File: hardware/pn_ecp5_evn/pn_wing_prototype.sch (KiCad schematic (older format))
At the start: 7 parts, among them J101 Screw_Terminal_01x02, J102 Conn_Coaxial, J103 Conn_02x20_Odd_Even, J104 Conn_Coaxial, J105 Conn_Coaxial, J106 Conn_Coaxial, J107 Conn_01x10

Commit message: first pass footprint assignment on pn r0
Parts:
- J101: footprint (none) -> TerminalBlock_Phoenix:TerminalBlock_Phoenix_MPT-0,5-2-2.54_1x02_P2.54mm_Horizontal
- J102: footprint (none) -> Connector_Coaxial:SMA_Molex_73251-1153_EdgeMount_Horizontal
- J103: footprint (none) -> Connector_PinSocket_2.54mm:PinSocket_2x20_P2.54mm_Vertical
- J104, J105, J106: footprint (none) -> Connector_Coaxial:SMA_Amphenol_132134_Vertical
- J107: footprint (none) -> Connector_PinHeader_2.54mm:PinHeader_1x10_P2.54mm_Vertical
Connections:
- net isolator/BUF_~PD~_ISO: now reaches J103.31 (Pin_31)
- no-connect marks 12 -> 11
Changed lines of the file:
@@
 F 0 "J102" H 1078 1988 50  0000 C CNN
 F 1 "Conn_Coaxial" H 1078 1897 50  0000 C CNN
-F 2 "" H 1150 1750 50  0001 C CNN
+F 2 "Connector_Coaxial:SMA_Molex_73251-1153_EdgeMount_Horizontal" H 1150 1750 50  0001 C CNN
 F 3 " ~" H 1150 1750 50  0001 C CNN
 	1    1150 1750
@@
 F4 "VOUT_P" I R 6700 1650 50
 F5 "VOUT_N" I R 6700 2150 50
+F6 "BUF_~PD" I R 6700 3050 50
 $EndSheet
 $Sheet
@@
 F20 "ADC_SCK" I R 7650 5250 50
 F21 "ADC_SDO" O R 7650 5350 50
+F22 "BUF_~PD" I L 6550 5450 50
+F23 "BUF_~PD~_ISO" O R 7650 5450 50
 $EndSheet
 Text Label 6350 3950 2    50   ~ 0
@@
 F 0 "J104" H 9250 1625 50  0000 L CNN
 F 1 "Conn_Coaxial" H 9250 1534 50  0000 L CNN
-F 2 "" H 9150 1650 50  0001 C CNN
+F 2 "Connector_Coaxial:SMA_Amphenol_132134_Vertical" H 9150 1650 50  0001 C CNN
 F 3 " ~" H 9150 1650 50  0001 C CNN
 	1    9150 1650
@@
 F 0 "J105" H 9250 2125 50  0000 L CNN
 F 1 "Conn_Coaxial" H 9250 2034 50  0000 L CNN
-F 2 "" H 9150 2150 50  0001 C CNN
+F 2 "Connector_Coaxial:SMA_Amphenol_132134_Vertical" H 9150 2150 50  0001 C CNN
 F 3 " ~" H 9150 2150 50  0001 C CNN
 	1    9150 2150
@@
 F 0 "J106" H 9250 2675 50  0000 L CNN
 F 1 "Conn_Coaxial" H 9250 2584 50  0000 L CNN
-F 2 "" H 9150 2700 50  0001 C CNN
+F 2 "Connector_Coaxial:SMA_Amphenol_132134_Vertical" H 9150 2700 50  0001 C CNN
 F 3 " ~" H 9150 2700 50  0001 C CNN
 	1    9150 2700
@@
 F 0 "J103" H 9100 5967 50  0000 C CNN
 F 1 "Conn_02x20_Odd_Even" H 9100 5876 50  0000 C CNN
-F 2 "" H 9050 4850 50  0001 C CNN
+F 2 "Connector_PinSocket_2.54mm:PinSocket_2x20_P2.54mm_Vertical" H 9050 4850 50  0001 C CNN
 F 3 "~" H 9050 4850 50  0001 C CNN
 	1    9050 4850
@@
 F 0 "J107" H 10150 4950 50  0000 L CNN
 F 1 "Conn_01x10" H 10050 4850 50  0000 L CNN
-F 2 "" H 10200 4350 50  0001 C CNN
+F 2 "Connector_PinHeader_2.54mm:PinHeader_1x10_P2.54mm_Vertical" H 10200 4350 50  0001 C CNN
 F 3 "~" H 10200 4350 50  0001 C CNN
 	1    10200 4350
@@
 NoConn ~ 8850 4250
 NoConn ~ 8850 4950
-NoConn ~ 8850 5450
 NoConn ~ 8850 5550
 NoConn ~ 8850 5650
@@
 F 0 "J101" H 1080 5342 50  0000 L CNN
 F 1 "Screw_Terminal_01x02" H 1080 5251 50  0000 L CNN
-F 2 "" H 1000 5350 50  0001 C CNN
+F 2 "TerminalBlock_Phoenix:TerminalBlock_Phoenix_MPT-0,5-2-2.54_1x02_P2.54mm_Horizontal" H 1000 5350 50  0001 C CNN
 F 3 "~" H 1000 5350 50  0001 C CNN
 	1    1000 5350
@@
 Wire Wire Line
 	1200 5350 1400 5350
+Wire Wire Line
+	7650 5450 8850 5450
+Wire Wire Line
+	6550 5450 6350 5450
+Text Label 6350 5450 2    50   ~ 0
+BUF_~PD
+Text Label 6850 3050 0    50   ~ 0
+BUF_~PD
+Wire Wire Line
+	6850 3050 6700 3050
 $EndSCHEMATC

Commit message: started component placement on phase noise analyzer
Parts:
- J102: footprint Connector_Coaxial:SMA_Molex_73251-1153_EdgeMount_Horizontal -> vna:SMA_Molex_73251-1153_OSHFR408
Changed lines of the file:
@@
 F 0 "J102" H 1078 1988 50  0000 C CNN
 F 1 "Conn_Coaxial" H 1078 1897 50  0000 C CNN
-F 2 "Connector_Coaxial:SMA_Molex_73251-1153_EdgeMount_Horizontal" H 1150 1750 50  0001 C CNN
+F 2 "vna:SMA_Molex_73251-1153_OSHFR408" H 1150 1750 50  0001 C CNN
 F 3 " ~" H 1150 1750 50  0001 C CNN
 	1    1150 1750

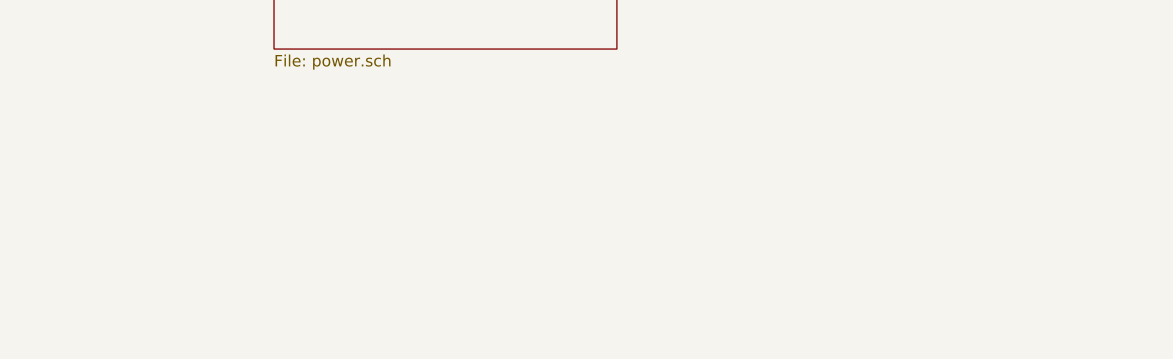
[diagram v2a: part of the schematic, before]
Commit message: component placement on phase noise downconverter
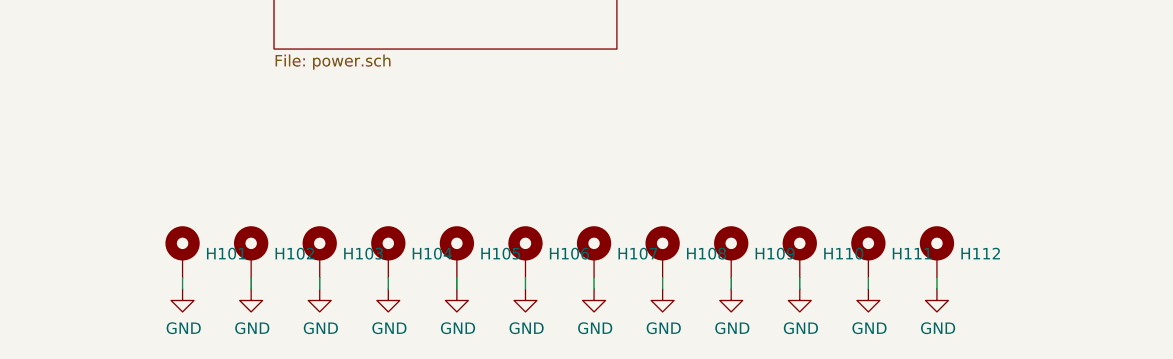
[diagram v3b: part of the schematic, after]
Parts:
- added H101, H102, H103, H104, H105, H106, H107, H108, H109, H110, H111, H112: MountingHole_Pad, MountingHole:MountingHole_2.7mm_M2.5_ISO14580_Pad, symbol Mechanical:MountingHole_Pad
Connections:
- net GND: now also H101.1, H102.1, H103.1, H104.1, H105.1, H106.1, H107.1, H108.1, H109.1, H110.1, H111.1, H112.1

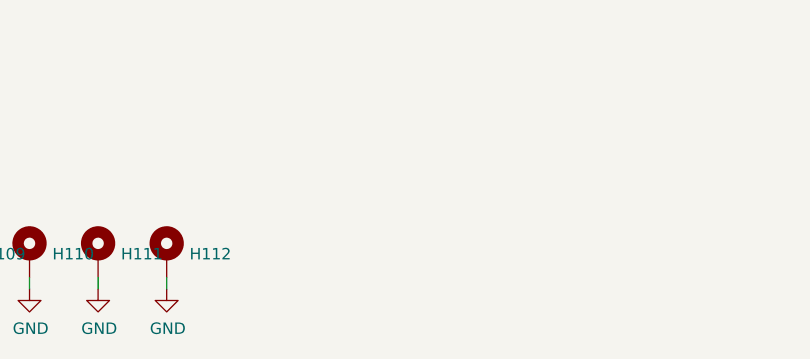
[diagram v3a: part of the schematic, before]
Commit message: first pass component placement on phase noise downconverter
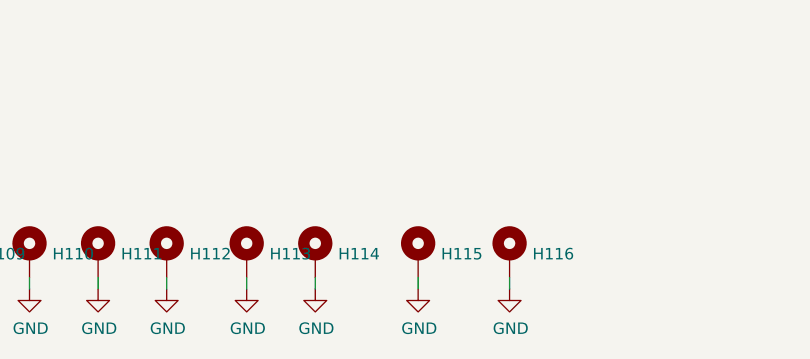
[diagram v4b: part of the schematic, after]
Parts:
- added H113, H114, H115, H116: MountingHole_Pad, MountingHole:MountingHole_2.7mm_M2.5_ISO14580_Pad, symbol Mechanical:MountingHole_Pad
- J104, J105, J106: footprint Connector_Coaxial:SMA_Amphenol_132134_Vertical -> vna:SMA_Molex_73251-1153_OSHFR408
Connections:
- net GND: now also H113.1, H114.1, H115.1, H116.1
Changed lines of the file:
@@
 F 0 "J104" H 9250 1625 50  0000 L CNN
 F 1 "Conn_Coaxial" H 9250 1534 50  0000 L CNN
-F 2 "Connector_Coaxial:SMA_Amphenol_132134_Vertical" H 9150 1650 50  0001 C CNN
+F 2 "vna:SMA_Molex_73251-1153_OSHFR408" H 9150 1650 50  0001 C CNN
 F 3 " ~" H 9150 1650 50  0001 C CNN
 	1    9150 1650
@@
 F 0 "J105" H 9250 2125 50  0000 L CNN
 F 1 "Conn_Coaxial" H 9250 2034 50  0000 L CNN
-F 2 "Connector_Coaxial:SMA_Amphenol_132134_Vertical" H 9150 2150 50  0001 C CNN
+F 2 "vna:SMA_Molex_73251-1153_OSHFR408" H 9150 2150 50  0001 C CNN
 F 3 " ~" H 9150 2150 50  0001 C CNN
 	1    9150 2150
@@
 F 0 "J106" H 9250 2675 50  0000 L CNN
 F 1 "Conn_Coaxial" H 9250 2584 50  0000 L CNN
-F 2 "Connector_Coaxial:SMA_Amphenol_132134_Vertical" H 9150 2700 50  0001 C CNN
+F 2 "vna:SMA_Molex_73251-1153_OSHFR408" H 9150 2700 50  0001 C CNN
 F 3 " ~" H 9150 2700 50  0001 C CNN
 	1    9150 2700
@@
 Wire Wire Line
 	4300 7550 4300 7600
+$Comp
+L Mechanical:MountingHole_Pad H113
+U 1 1 5F4447D1
+P 4650 7450
+F 0 "H113" H 4750 7453 50  0000 L CNN
+F 1 "MountingHole_Pad" H 4750 7408 50  0001 L CNN
+F 2 "MountingHole:MountingHole_2.7mm_M2.5_ISO14580_Pad" H 4650 7450 50  0001 C CNN
+F 3 "~" H 4650 7450 50  0001 C CNN
+	1    4650 7450
+	1    0    0    -1
+$EndComp
+$Comp
+L power:GND #PWR0301
+U 1 1 5F4447D7
+P 4650 7600
+F 0 "#PWR0301" H 4650 7350 50  0001 C CNN
+F 1 "GND" H 4655 7427 50  0000 C CNN
+F 2 "" H 4650 7600 50  0001 C CNN
+F 3 "" H 4650 7600 50  0001 C CNN
+	1    4650 7600
+	1    0    0    -1
+$EndComp
+Wire Wire Line
+	4650 7550 4650 7600
+$Comp
+L Mechanical:MountingHole_Pad H114
+U 1 1 5F4447DE
+P 4950 7450
+F 0 "H114" H 5050 7453 50  0000 L CNN
+F 1 "MountingHole_Pad" H 5050 7408 50  0001 L CNN
+F 2 "MountingHole:MountingHole_2.7mm_M2.5_ISO14580_Pad" H 4950 7450 50  0001 C CNN
+F 3 "~" H 4950 7450 50  0001 C CNN
+	1    4950 7450
+	1    0    0    -1
+$EndComp
+$Comp
+L power:GND #PWR0302
+U 1 1 5F4447E4
+P 4950 7600
+F 0 "#PWR0302" H 4950 7350 50  0001 C CNN
+F 1 "GND" H 4955 7427 50  0000 C CNN
+F 2 "" H 4950 7600 50  0001 C CNN
+F 3 "" H 4950 7600 50  0001 C CNN
+	1    4950 7600
+	1    0    0    -1
+$EndComp
+Wire Wire Line
+	4950 7550 4950 7600
+$Comp
+L Mechanical:MountingHole_Pad H115
+U 1 1 5F4575A6
+P 5400 7450
+F 0 "H115" H 5500 7453 50  0000 L CNN
+F 1 "MountingHole_Pad" H 5500 7408 50  0001 L CNN
+F 2 "MountingHole:MountingHole_2.7mm_M2.5_ISO14580_Pad" H 5400 7450 50  0001 C CNN
+F 3 "~" H 5400 7450 50  0001 C CNN
+	1    5400 7450
+	1    0    0    -1
+$EndComp
+$Comp
+L power:GND #PWR0303
+U 1 1 5F4575AC
+P 5400 7600
+F 0 "#PWR0303" H 5400 7350 50  0001 C CNN
+F 1 "GND" H 5405 7427 50  0000 C CNN
+F 2 "" H 5400 7600 50  0001 C CNN
+F 3 "" H 5400 7600 50  0001 C CNN
+	1    5400 7600
+	1    0    0    -1
+$EndComp
+Wire Wire Line
+	5400 7550 5400 7600
+$Comp
+L Mechanical:MountingHole_Pad H116
+U 1 1 5F475610
+P 5800 7450
+F 0 "H116" H 5900 7453 50  0000 L CNN
+F 1 "MountingHole_Pad" H 5900 7408 50  0001 L CNN
+F 2 "MountingHole:MountingHole_2.7mm_M2.5_ISO14580_Pad" H 5800 7450 50  0001 C CNN
+F 3 "~" H 5800 7450 50  0001 C CNN
+	1    5800 7450
+	1    0    0    -1
+$EndComp
+$Comp
+L power:GND #PWR0304
+U 1 1 5F475616
+P 5800 7600
+F 0 "#PWR0304" H 5800 7350 50  0001 C CNN
+F 1 "GND" H 5805 7427 50  0000 C CNN
+F 2 "" H 5800 7600 50  0001 C CNN
+F 3 "" H 5800 7600 50  0001 C CNN
+	1    5800 7600
+	1    0    0    -1
+$EndComp
+Wire Wire Line
+	5800 7550 5800 7600
 $EndSCHEMATC

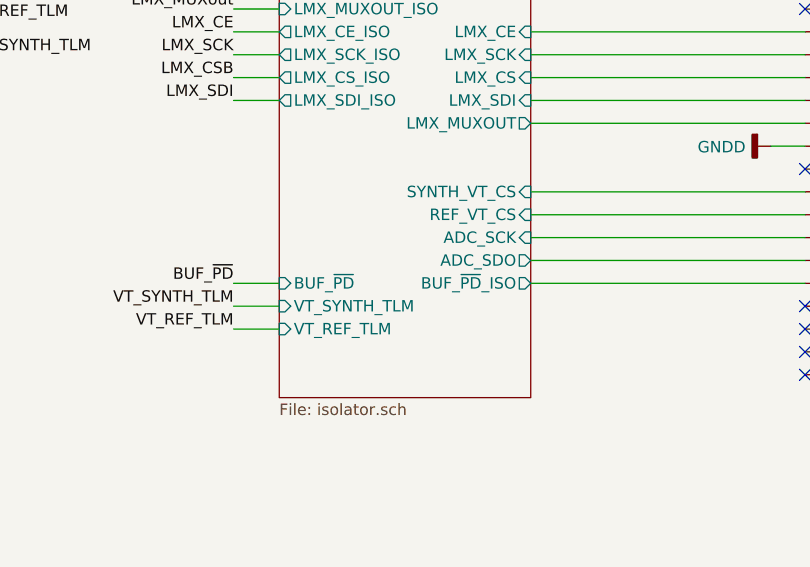
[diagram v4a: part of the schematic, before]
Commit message: work on routing phase noise downconverter
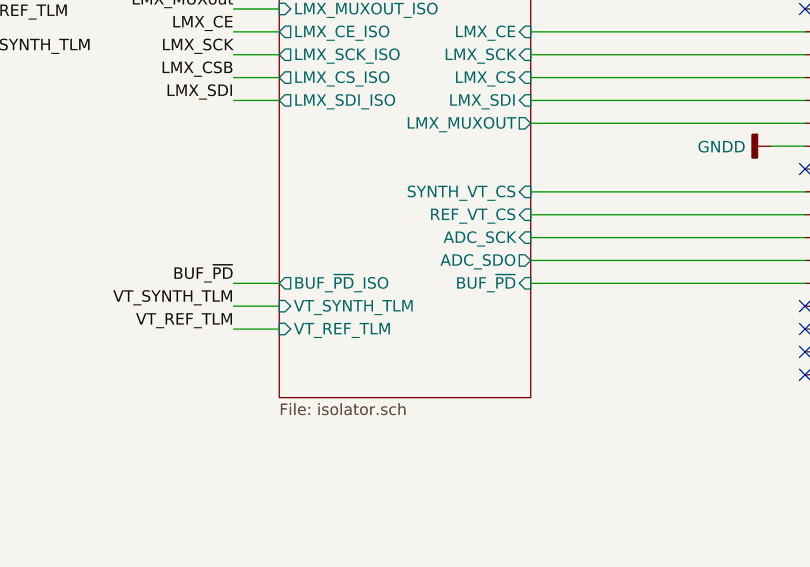
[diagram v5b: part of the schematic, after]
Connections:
- net isolator/BUF_~PD~_ISO renamed isolator/BUF_~PD
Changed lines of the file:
@@
 F20 "ADC_SCK" I R 7650 5250 50
 F21 "ADC_SDO" O R 7650 5350 50
-F22 "BUF_~PD" I L 6550 5450 50
-F23 "BUF_~PD~_ISO" O R 7650 5450 50
+F22 "BUF_~PD" I R 7650 5450 50
+F23 "BUF_~PD~_ISO" O L 6550 5450 50
 $EndSheet
 Text Label 6350 3950 2    50   ~ 0

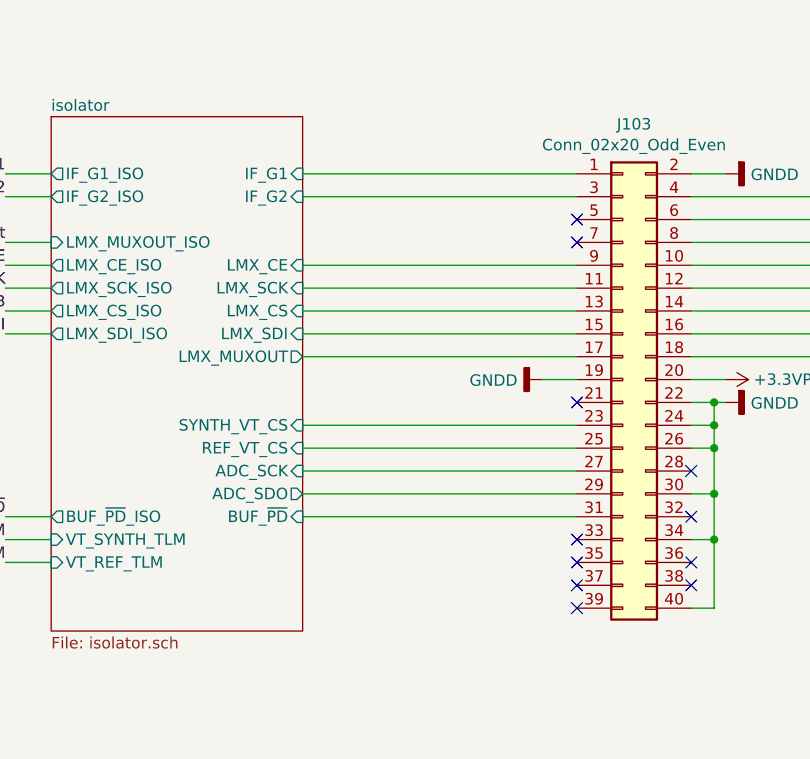
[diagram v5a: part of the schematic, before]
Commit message: layout of phase noise downconverter
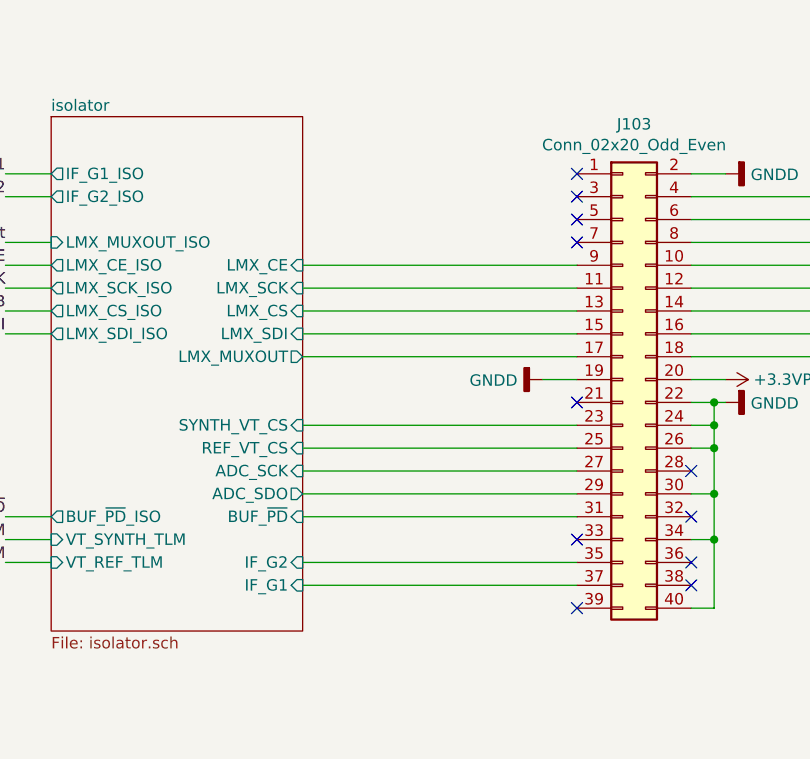
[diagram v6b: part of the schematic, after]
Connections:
- net isolator/IF_G1: now also J103.37 (Pin_37); no longer J103.1 (Pin_1)
- net isolator/IF_G2: now also J103.35 (Pin_35); no longer J103.3 (Pin_3)
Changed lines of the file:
@@
 F6 "LMX_CS_ISO" O L 6550 4550 50
 F7 "LMX_SDI_ISO" O L 6550 4650 50
-F8 "IF_G1" I R 7650 3950 50
-F9 "IF_G2" I R 7650 4050 50
+F8 "IF_G1" I R 7650 5750 50
+F9 "IF_G2" I R 7650 5650 50
 F10 "LMX_CE" I R 7650 4350 50
 F11 "LMX_SCK" I R 7650 4450 50
@@
 	9500 4850 9350 4850
 Wire Wire Line
-	7650 3950 8850 3950
-Wire Wire Line
-	7650 4050 8850 4050
-Wire Wire Line
 	7650 4350 8850 4350
 Wire Wire Line
@@
 NoConn ~ 8850 4950
 NoConn ~ 8850 5550
-NoConn ~ 8850 5650
-NoConn ~ 8850 5750
 NoConn ~ 8850 5850
 NoConn ~ 9350 5750
@@
 Wire Wire Line
 	5800 7550 5800 7600
+NoConn ~ 8850 3950
+NoConn ~ 8850 4050
+Wire Wire Line
+	8850 5650 7650 5650
+Wire Wire Line
+	7650 5750 8850 5750
 $EndSCHEMATC

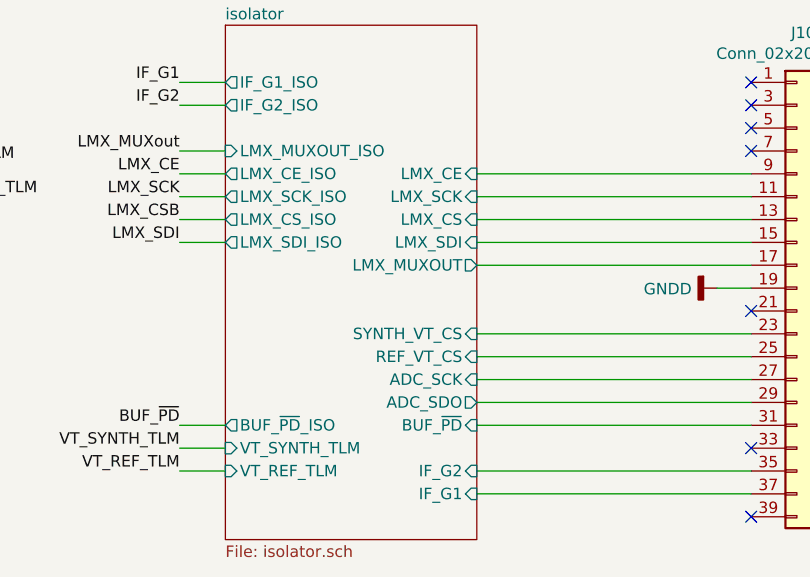
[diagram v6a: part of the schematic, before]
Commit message: all nets connected in layout
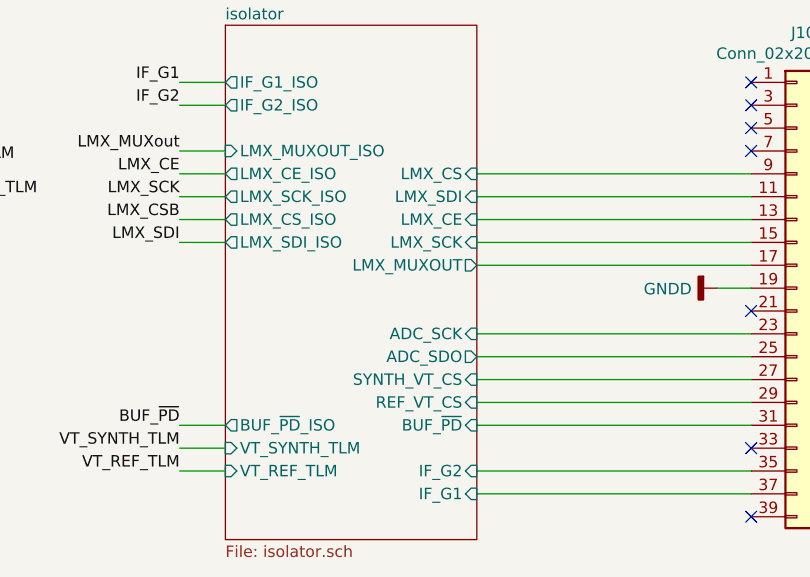
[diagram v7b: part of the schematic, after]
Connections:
- net isolator/ADC_SCK: now also J103.23 (Pin_23); no longer J103.27 (Pin_27)
- net isolator/ADC_SDO: now also J103.25 (Pin_25); no longer J103.29 (Pin_29)
- net isolator/LMX_CE: now also J103.13 (Pin_13); no longer J103.9 (Pin_9)
- net isolator/LMX_CS: now also J103.9 (Pin_9); no longer J103.13 (Pin_13)
- net isolator/LMX_SCK: now also J103.15 (Pin_15); no longer J103.11 (Pin_11)
- net isolator/LMX_SDI: now also J103.11 (Pin_11); no longer J103.15 (Pin_15)
- net isolator/REF_VT_CS: now also J103.29 (Pin_29); no longer J103.25 (Pin_25)
- net isolator/SYNTH_VT_CS: now also J103.27 (Pin_27); no longer J103.23 (Pin_23)
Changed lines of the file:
@@
 F8 "IF_G1" I R 7650 5750 50
 F9 "IF_G2" I R 7650 5650 50
-F10 "LMX_CE" I R 7650 4350 50
-F11 "LMX_SCK" I R 7650 4450 50
-F12 "LMX_CS" I R 7650 4550 50
-F13 "LMX_SDI" I R 7650 4650 50
-F14 "SYNTH_VT_CS" I R 7650 5050 50
-F15 "REF_VT_CS" I R 7650 5150 50
+F10 "LMX_CE" I R 7650 4550 50
+F11 "LMX_SCK" I R 7650 4650 50
+F12 "LMX_CS" I R 7650 4350 50
+F13 "LMX_SDI" I R 7650 4450 50
+F14 "SYNTH_VT_CS" I R 7650 5250 50
+F15 "REF_VT_CS" I R 7650 5350 50
 F16 "VT_SYNTH_TLM" I L 6550 5550 50
 F17 "VT_REF_TLM" I L 6550 5650 50
 F18 "LMX_MUXOUT_ISO" I L 6550 4250 50
 F19 "LMX_MUXOUT" O R 7650 4750 50
-F20 "ADC_SCK" I R 7650 5250 50
-F21 "ADC_SDO" O R 7650 5350 50
+F20 "ADC_SCK" I R 7650 5050 50
+F21 "ADC_SDO" O R 7650 5150 50
 F22 "BUF_~PD" I R 7650 5450 50
 F23 "BUF_~PD~_ISO" O L 6550 5450 50

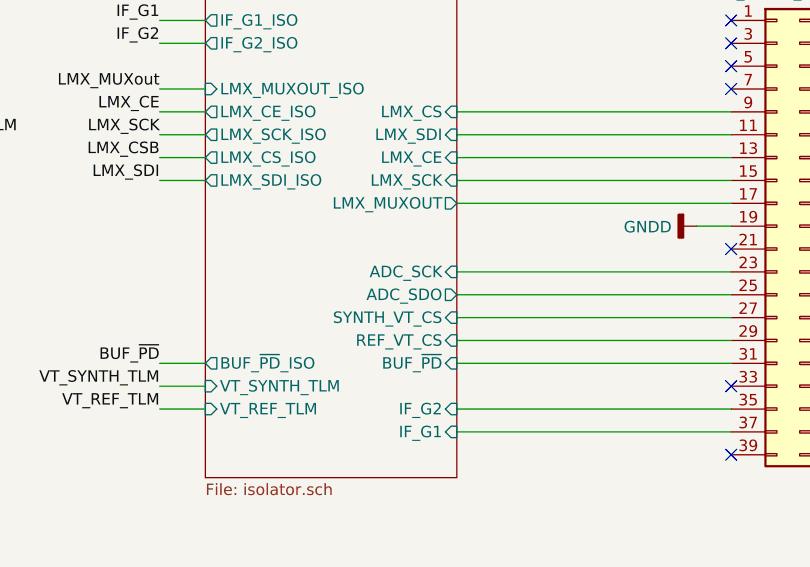
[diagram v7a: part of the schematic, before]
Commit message: drc and erc check, schematic cleanup
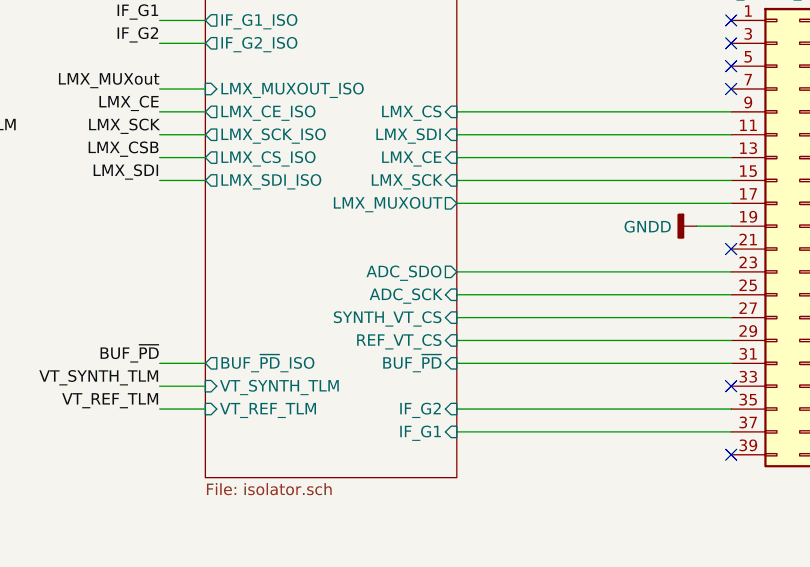
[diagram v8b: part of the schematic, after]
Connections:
- net isolator/ADC_SCK: now also J103.25 (Pin_25); no longer J103.23 (Pin_23)
- net isolator/ADC_SDO: now also J103.23 (Pin_23); no longer J103.25 (Pin_25)
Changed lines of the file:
@@
 F18 "LMX_MUXOUT_ISO" I L 6550 4250 50
 F19 "LMX_MUXOUT" O R 7650 4750 50
-F20 "ADC_SCK" I R 7650 5050 50
-F21 "ADC_SDO" O R 7650 5150 50
+F20 "ADC_SCK" I R 7650 5150 50
+F21 "ADC_SDO" O R 7650 5050 50
 F22 "BUF_~PD" I R 7650 5450 50
 F23 "BUF_~PD~_ISO" O L 6550 5450 50
